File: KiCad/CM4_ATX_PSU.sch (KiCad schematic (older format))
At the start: 2 parts, among them J7 39-28-1243

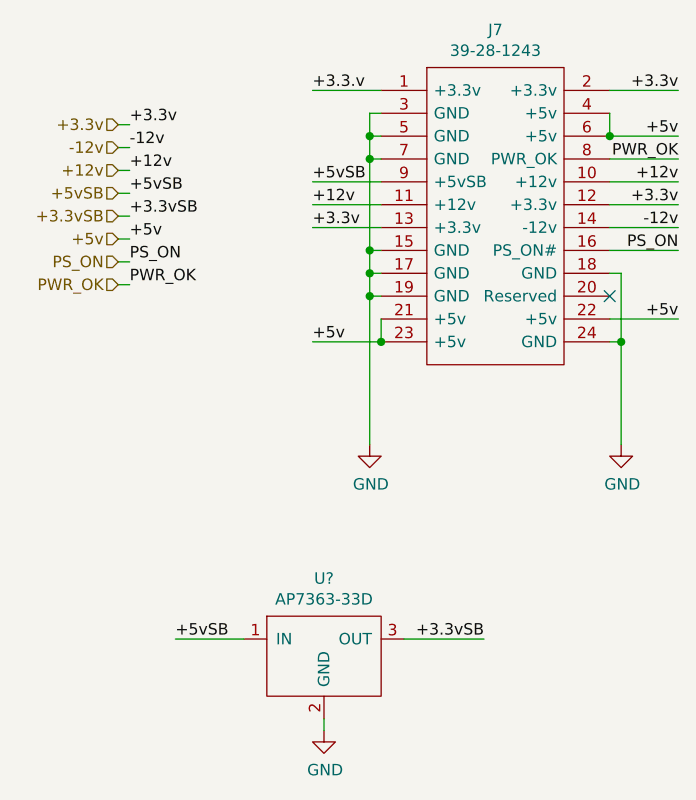
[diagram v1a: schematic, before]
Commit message: updated part numerations
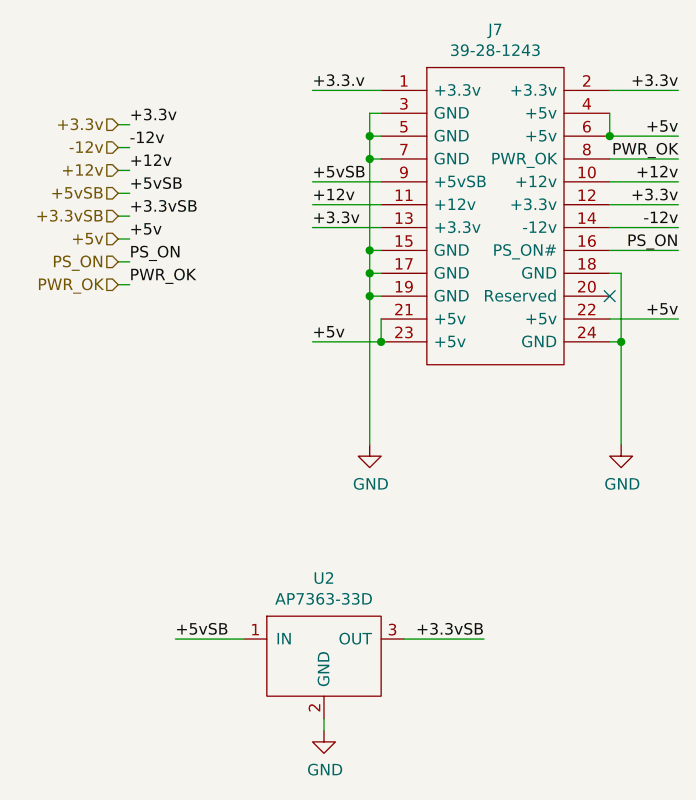
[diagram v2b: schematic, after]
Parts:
- gave numbers to parts that had none: 1
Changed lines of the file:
@@
 +5vSB
 $Comp
-L CM4_MATX:AP7363-33D U?
+L CM4_MATX:AP7363-33D U2
 U 1 1 5FEC8807
 P 5700 5950
-F 0 "U?" H 5700 6215 50  0000 C CNN
+F 0 "U2" H 5700 6215 50  0000 C CNN
 F 1 "AP7363-33D" H 5700 6124 50  0000 C CNN
 F 2 "" H 5700 5950 50  0001 C CNN
